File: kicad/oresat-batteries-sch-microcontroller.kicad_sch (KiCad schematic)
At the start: 28 parts, among them J2 SM14B-SHLS-TF, U20 TCAN330, U21 STM32F091C, X3 ECS-160-10-36Q-ES-TR

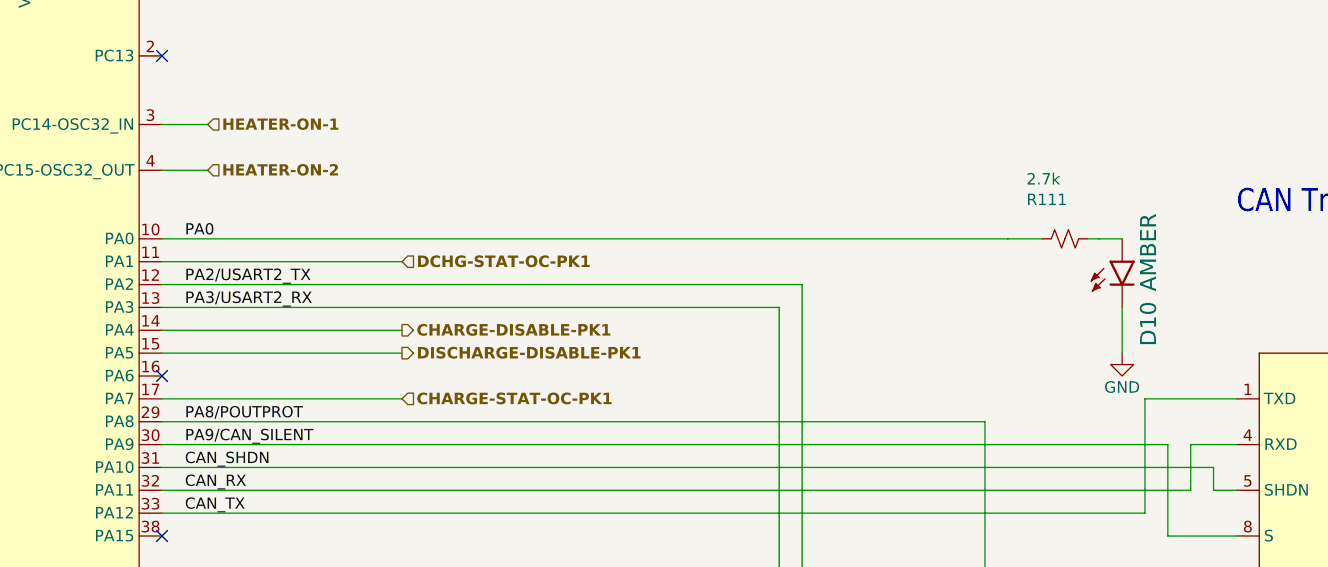
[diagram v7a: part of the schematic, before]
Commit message: Progress on battery card v4
Moved in -batt cutoffs, which caused a lot of pain and suffering. Started updating BOM, and fixed all transistor packages. Updated resistor packages, too. Still needs a lot of cleanup, but probably 80% done now.
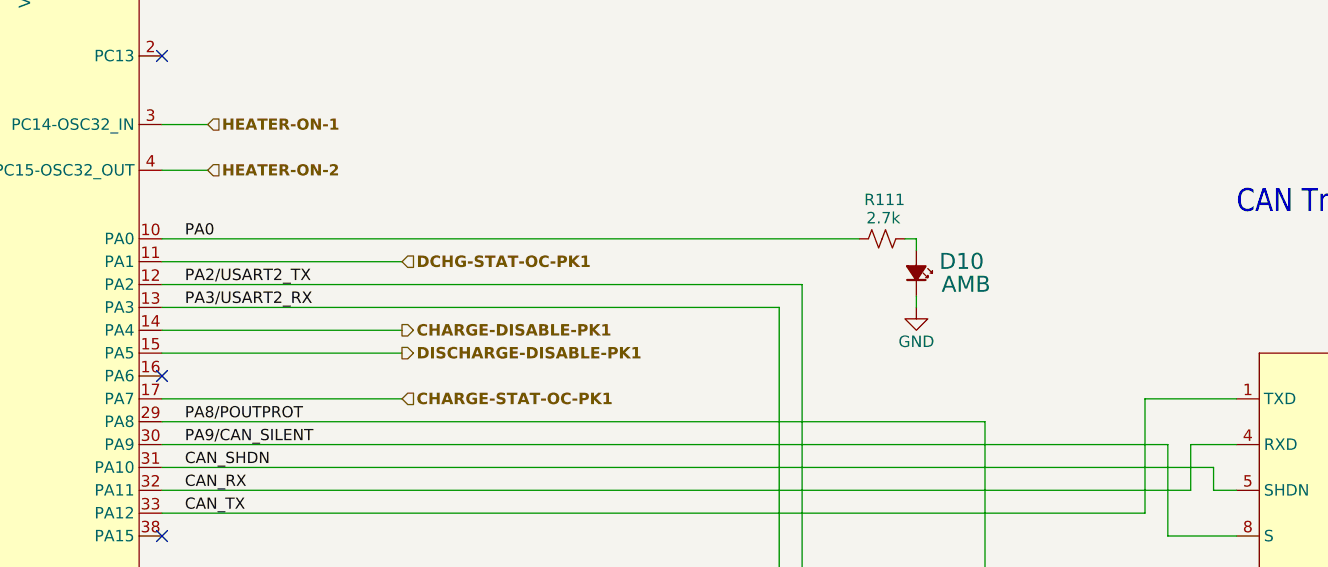
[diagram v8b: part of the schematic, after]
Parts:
- C44, C45, C46, C47, C48, C49, C50: footprint oresat-passives:c_0603-SMALL -> oresat-passives:0603-C-NOSILK
- D10: value AMBER -> AMB; footprint oresat-batteries:LED-0603 -> LED_SMD:LED_0603_1608Metric; symbol oresat-batteries-eagle-import:LED-GREEN0603 -> Device:LED_Small_Filled
- R110, R111, R112, R113, R114, R63, R64, R68, R72: footprint oresat-batteries:.0603-C-NOSILK -> oresat-passives:0603-C-NOSILK
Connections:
- net GND: now also D10.1 (K); no longer D10.C
- net at R111.1: now also D10.2 (A); no longer D10.A
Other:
- moved on the sheet: R111
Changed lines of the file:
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@@
 	(wire
 		(pts
-			(xy 358.14 81.28) (xy 360.68 81.28)
-		)
-		(stroke
-			(width 0.1524)
-			(type solid)
-		)
-	)
-	(wire
-		(pts
 			(xy 365.76 104.14) (xy 365.76 114.3)
 		)
@@
 	(wire
 		(pts
-			(xy 360.68 88.9) (xy 360.68 93.98)
-		)
-		(stroke
-			(width 0.1524)
-			(type solid)
-		)
-	)
-	(wire
-		(pts
 			(xy 48.26 160.02) (xy 48.26 157.48)
 		)
@@
 	(wire
 		(pts
-			(xy 356.87 81.28) (xy 358.14 81.28)
+			(xy 336.55 81.28) (xy 337.82 81.28)
 		)
 		(stroke
@@
 	(wire
 		(pts
+			(xy 337.82 81.28) (xy 337.82 82.55)
+		)
+		(stroke
+			(width 0)
+			(type default)
+		)
+	)
+	(wire
+		(pts
 			(xy 254 93.98) (xy 280.67 93.98)
 		)
@@
 	(wire
 		(pts
+			(xy 337.82 87.63) (xy 337.82 88.9)
+		)
+		(stroke
+			(width 0)
+			(type default)
+		)
+	)
+	(wire
+		(pts
 			(xy 148.59 100.33) (xy 151.13 100.33)
 		)
@@
 	(wire
 		(pts
-			(xy 351.79 81.28) (xy 347.98 81.28)
-		)
-		(stroke
-			(width 0)
-			(type default)
-		)
-	)
-	(wire
-		(pts
 			(xy 33.02 68.58) (xy 33.02 71.12)
 		)
@@
 	(wire
 		(pts
-			(xy 254 81.28) (xy 347.98 81.28)
+			(xy 254 81.28) (xy 331.47 81.28)
 		)
 		(stroke
@@
 			)
 		)
-		(property "Footprint" "oresat-passives:c_0603-SMALL"
+		(property "Footprint" "oresat-passives:0603-C-NOSILK"
 			(at 231.14 30.48 0)
 			(effects
@@
 	(symbol
 		(lib_id "Device:R_Small_US")
-		(at 354.33 81.28 270)
+		(at 334.01 81.28 270)
 		(unit 1)
 		(exclude_from_sim no)
@@
 		(dnp no)
 		(property "Reference" "R111"
-			(at 354.584 76.2 90)
+			(at 336.55 76.2 90)
 			(effects
 				(font
@@
 		)
 		(property "Value" "2.7k"
-			(at 353.822 73.914 90)
+			(at 336.042 78.232 90)
 			(effects
 				(font
@@
 			)
 		)
-		(property "Footprint" "oresat-batteries:.0603-C-NOSILK"
-			(at 354.33 81.28 0)
+		(property "Footprint" "oresat-passives:0603-C-NOSILK"
+			(at 334.01 81.28 0)
 			(effects
 				(font
@@
 		)
 		(property "Datasheet" "~"
-			(at 354.33 81.28 0)
+			(at 334.01 81.28 0)
 			(effects
 				(font
@@
 		)
 		(property "Description" "Resistor, small US symbol"
-			(at 354.33 81.28 0)
+			(at 334.01 81.28 0)
 			(effects
 				(font
@@
 		)
 		(property "DIS" "Digi-Key"
-			(at 354.33 81.28 0)
+			(at 334.01 81.28 0)
 			(effects
 				(font
@@
 		)
 		(property "DPN" "A129693CT-ND"
-			(at 354.33 81.28 0)
+			(at 334.01 81.28 0)
 			(effects
 				(font
@@
 		)
 		(property "MFR" "TE"
-			(at 354.33 81.28 0)
+			(at 334.01 81.28 0)
 			(effects
 				(font
@@
 		)
 		(property "MPN" "CRGCQ0603F2K7"
-			(at 354.33 81.28 0)
+			(at 334.01 81.28 0)
 			(effects
 				(font
@@
 			)
 		)
-		(property "Footprint" "oresat-batteries:.0603-C-NOSILK"
+		(property "Footprint" "oresat-passives:0603-C-NOSILK"
 			(at 50.8 71.12 0)
 			(effects
@@
 			)
 		)
-		(property "Footprint" "oresat-passives:c_0603-SMALL"
+		(property "Footprint" "oresat-passives:0603-C-NOSILK"
 			(at 396.24 88.9 0)
 			(effects
@@
 			)
 		)
-		(property "Footprint" "oresat-passives:c_0603-SMALL"
+		(property "Footprint" "oresat-passives:0603-C-NOSILK"
 			(at 210.82 30.48 0)
 			(effects
@@
 			)
 		)
-		(property "Footprint" "oresat-batteries:.0603-C-NOSILK"
+		(property "Footprint" "oresat-passives:0603-C-NOSILK"
 			(at 146.05 107.95 0)
 			(effects
@@
 			)
 		)
-		(property "Footprint" "oresat-batteries:.0603-C-NOSILK"
+		(property "Footprint" "oresat-passives:0603-C-NOSILK"
 			(at 109.22 97.79 0)
 			(effects
@@
 			)
 		)
-		(property "Footprint" "oresat-passives:c_0603-SMALL"
+		(property "Footprint" "oresat-passives:0603-C-NOSILK"
 			(at 138.43 41.91 0)
 			(effects
@@
 			)
 		)
-		(property "Footprint" "oresat-passives:c_0603-SMALL"
+		(property "Footprint" "oresat-passives:0603-C-NOSILK"
 			(at 218.44 30.48 0)
 			(effects
@@
 			)
 		)
-		(property "Footprint" "oresat-passives:c_0603-SMALL"
+		(property "Footprint" "oresat-passives:0603-C-NOSILK"
 			(at 146.05 41.91 0)
 			(effects
@@
 			)
 		)
-		(property "Footprint" "oresat-passives:c_0603-SMALL"
+		(property "Footprint" "oresat-passives:0603-C-NOSILK"
 			(at 243.84 30.48 0)
 			(effects
@@
 			)
 		)
-		(property "Footprint" "oresat-batteries:.0603-C-NOSILK"
+		(property "Footprint" "oresat-passives:0603-C-NOSILK"
 			(at 27.94 66.04 0)
 			(effects
@@
 			)
 		)
-		(property "Footprint" "oresat-batteries:.0603-C-NOSILK"
+		(property "Footprint" "oresat-passives:0603-C-NOSILK"
 			(at 345.44 162.56 0)
 			(effects
@@
 	(symbol
 		(lib_id "power:GND")
-		(at 360.68 93.98 0)
+		(at 337.82 88.9 0)
 		(mirror y)
 		(unit 1)
@@
 		(dnp no)
 		(property "Reference" "#PWR98"
-			(at 360.68 100.33 0)
+			(at 337.82 95.25 0)
 			(effects
 				(font
@@
 		)
 		(property "Value" "GND"
-			(at 360.68 97.79 0)
+			(at 337.82 92.71 0)
 			(effects
 				(font
@@
 		)
 		(property "Footprint" ""
-			(at 360.68 93.98 0)
+			(at 337.82 88.9 0)
 			(effects
 				(font
@@
 		)
 		(property "Datasheet" ""
-			(at 360.68 93.98 0)
+			(at 337.82 88.9 0)
 			(effects
 				(font
@@
 		)
 		(property "Description" "Power symbol creates a global label with name \"GND\" , ground"
-			(at 360.68 93.98 0)
+			(at 337.82 88.9 0)
 			(effects
 				(font
@@
 			)
 		)
-		(property "DIST" ""
-			(at 33.02 179.07 0)
-			(effects
-				(font
-					(size 1.27 1.27)
-				)
-				(hide yes)
-			)
-		)
 		(pin "3"
 		)
@@
 	)
 	(symbol
-		(lib_id "oresat-batteries-eagle-import:LED-GREEN0603")
-		(at 360.68 83.82 0)
+		(lib_id "Device:LED_Small_Filled")
+		(at 337.82 85.09 270)
+		(mirror x)
 		(unit 1)
 		(exclude_from_sim no)
@@
 		(dnp no)
 		(property "Reference" "D10"
-			(at 362.585 93.218 90)
+			(at 340.36 84.836 90)
 			(effects
 				(font
@@
 			)
 		)
-		(property "Value" "AMBER"
-			(at 362.585 87.122 90)
+		(property "Value" "AMB"
+			(at 340.614 87.376 90)
 			(effects
 				(font
@@
 			)
 		)
-		(property "Footprint" "oresat-batteries:LED-0603"
-			(at 360.68 83.82 0)
+		(property "Footprint" "LED_SMD:LED_0603_1608Metric"
+			(at 337.82 85.09 90)
 			(effects
 				(font
@@
 			)
 		)
-		(property "Datasheet" ""
-			(at 360.68 83.82 0)
+		(property "Datasheet" "~"
+			(at 337.82 85.09 90)
 			(effects
 				(font
@@
 			)
 		)
-		(property "Description" ""
-			(at 360.68 83.82 0)
+		(property "Description" "Light emitting diode, small symbol, filled shape"
+			(at 337.82 85.09 0)
 			(effects
 				(font
 					(size 1.27 1.27)
 				)
+				(hide yes)
 			)
 		)
 		(property "DIS" "Digi-Key"
-			(at 360.68 83.82 0)
+			(at 337.82 85.09 0)
 			(effects
 				(font
@@
 		)
 		(property "DPN" "1830-1064-1-ND"
-			(at 360.68 83.82 0)
+			(at 337.82 85.09 0)
 			(effects
 				(font
@@
 		)
 		(property "MFR" "Inolux"
-			(at 360.68 83.82 0)
+			(at 337.82 85.09 0)
 			(effects
 				(font
@@
 		)
 		(property "MPN" "IN-S63AT5A"
-			(at 360.68 83.82 0)
+			(at 337.82 85.09 0)
 			(effects
 				(font
@@
 			)
 		)
-		(pin "A"
+		(property "Sim.Pins" "1=K 2=A"
+			(at 337.82 85.09 0)
+			(effects
+				(font
+					(size 1.27 1.27)
+				)
+				(hide yes)
+			)
 		)
-		(pin "C"
+		(pin "1"
+		)
+		(pin "2"
 		)
 		(instances
@@
 			)
 		)
-		(property "Footprint" "oresat-batteries:.0603-C-NOSILK"
+		(property "Footprint" "oresat-passives:0603-C-NOSILK"
 			(at 151.13 107.95 0)
 			(effects
@@
 			)
 		)
-		(property "Footprint" "oresat-batteries:.0603-C-NOSILK"
+		(property "Footprint" "oresat-passives:0603-C-NOSILK"
 			(at 33.02 66.04 0)
 			(effects
@@
 			)
 		)
-		(property "Footprint" "oresat-batteries:.0603-C-NOSILK"
+		(property "Footprint" "oresat-passives:0603-C-NOSILK"
 			(at 116.84 97.79 0)
 			(effects
